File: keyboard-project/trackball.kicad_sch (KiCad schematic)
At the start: 0 parts

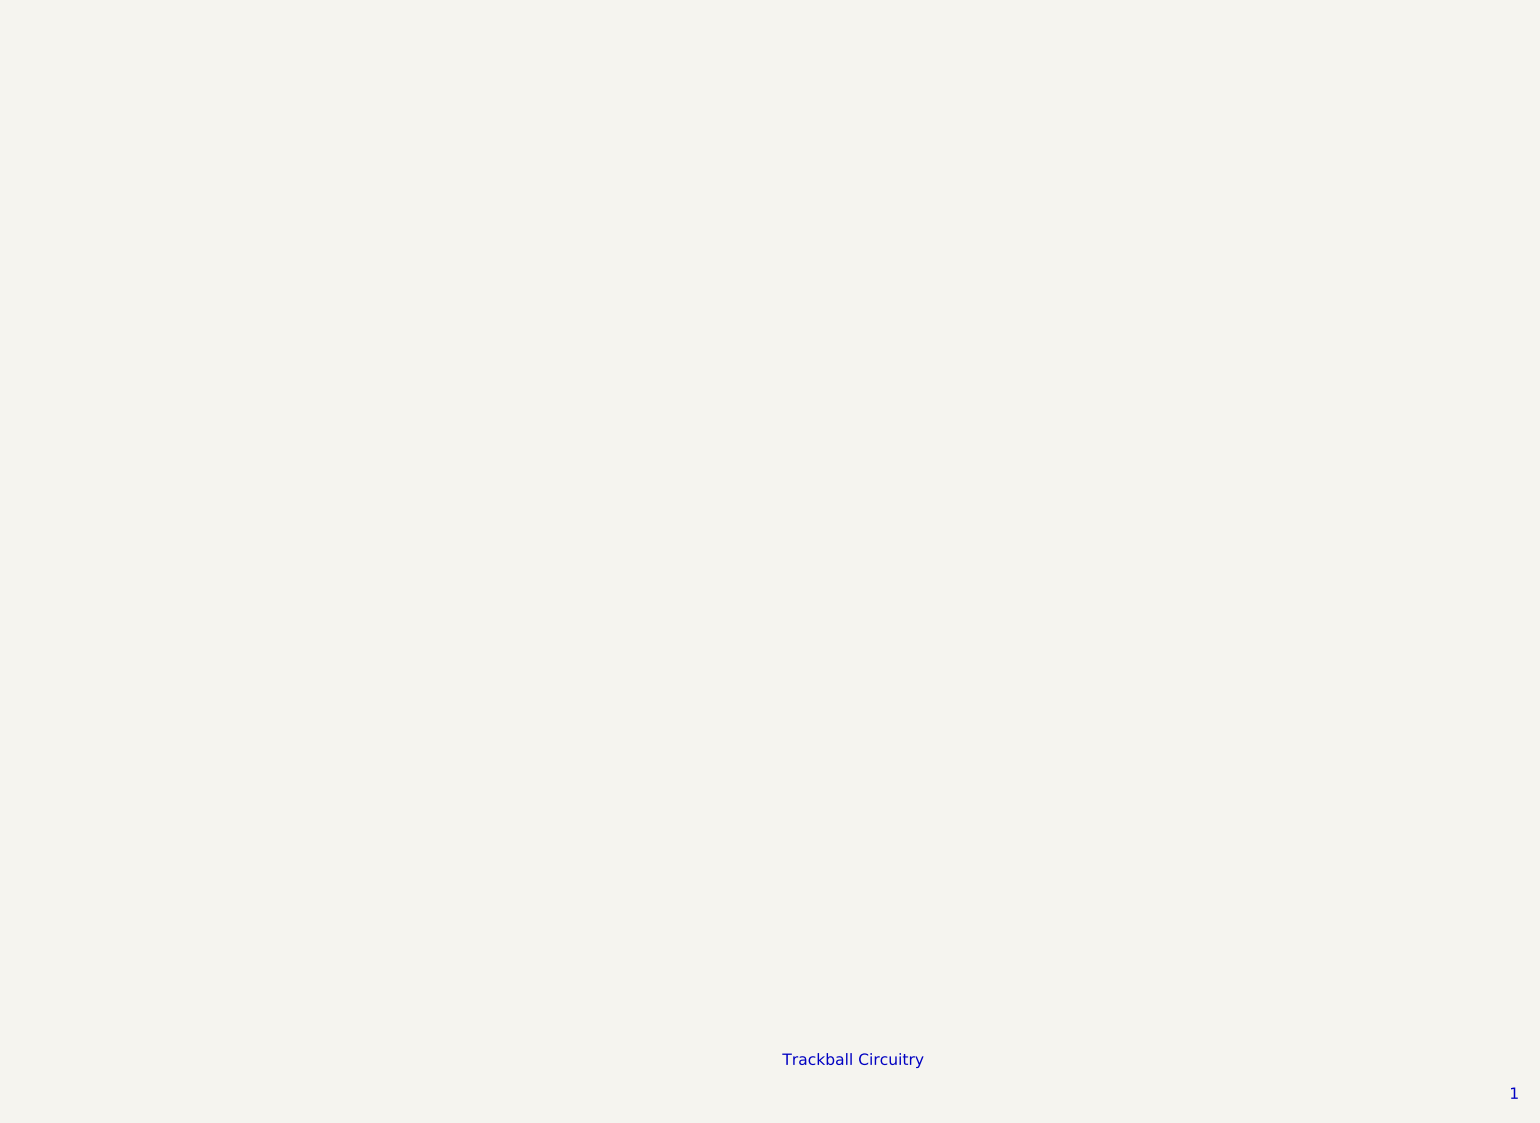
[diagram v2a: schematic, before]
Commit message: encoders, trackball, and display circuits
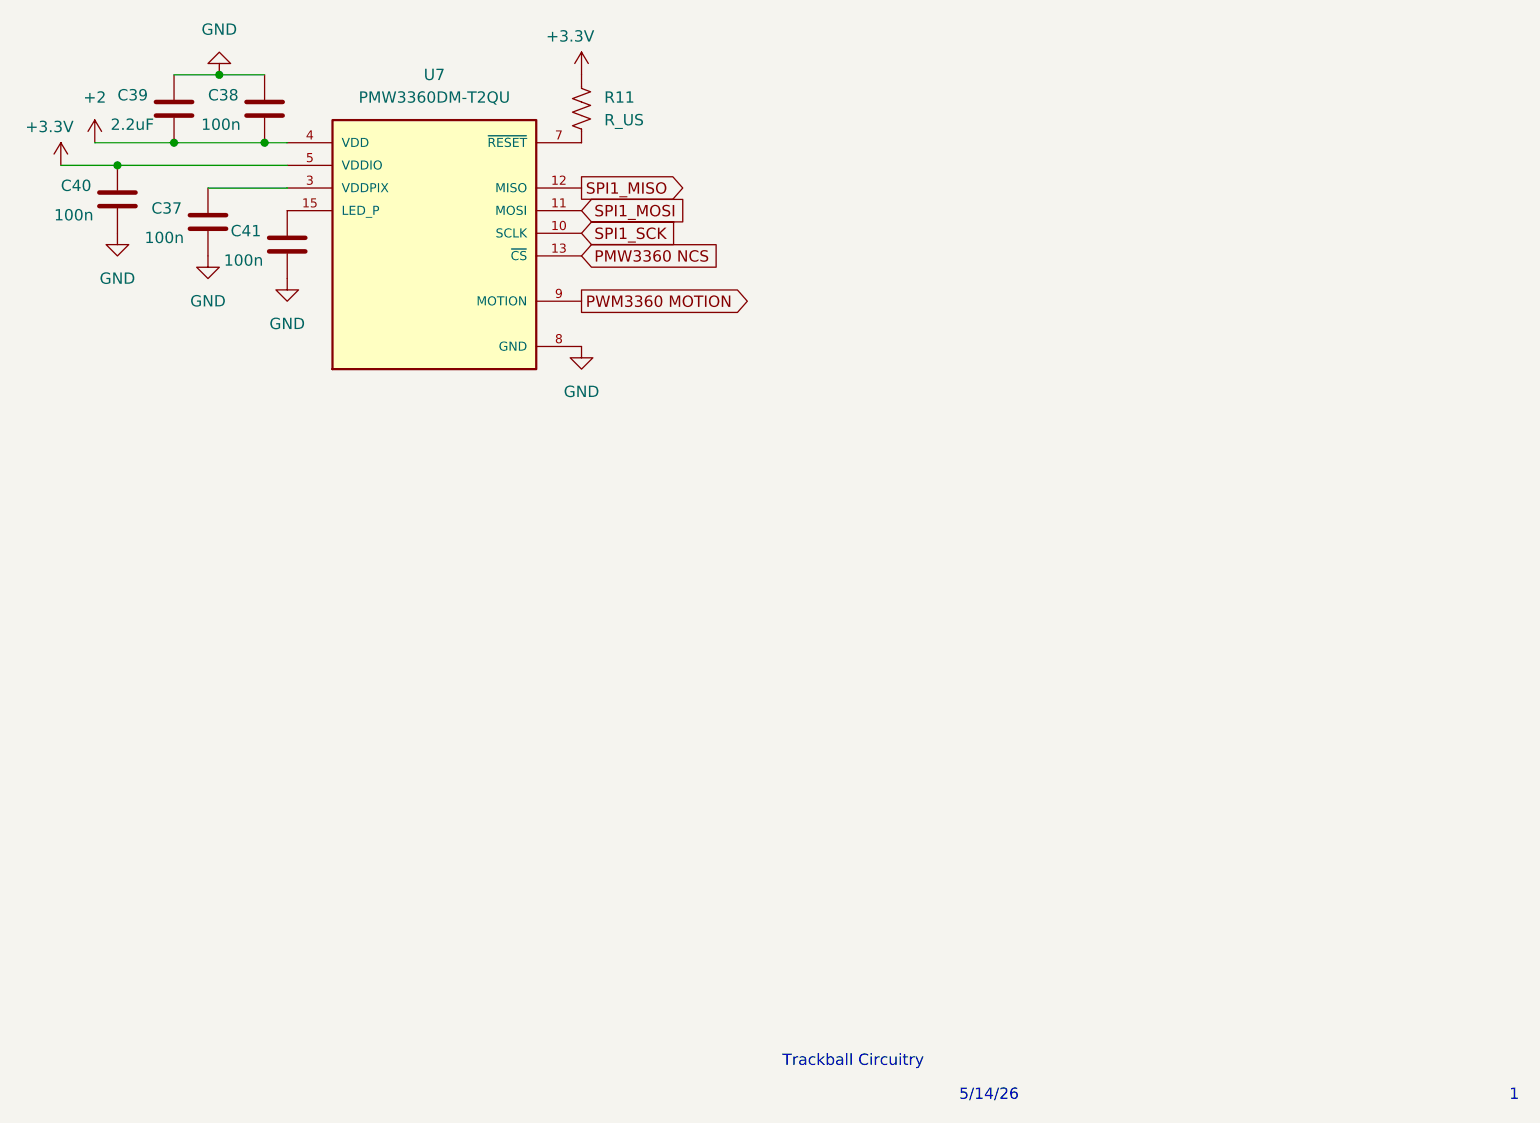
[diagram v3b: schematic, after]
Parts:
- added C37, C38, C40, C41: 100n, symbol Device:C
- added C39: 2.2uF, symbol Device:C
- added R11: R_US, symbol Device:R_US
- added U7: PMW3360DM-T2QU, symbol PMW3360DM-T2QU:PMW3360DM-T2QU
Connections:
- new net: C41.1, U7.15 (LED_P)
- new net: R11.2, U7.7 (~{RESET})
- new net: C37.1, U7.3 (VDDPIX)
- new net +2: C38.2, C39.2, U7.4 (VDD)
- new net +3.3V: C40.1, R11.1, U7.5 (VDDIO)
- new net GND: C37.2, C38.1, C39.1, C40.2, C41.2, U7.8 (GND)
- new net PMW3360 NCS: U7.13 (~{CS})
- new net PWM3360 MOTION: U7.9 (MOTION)
- new net SPI1_MISO: U7.12 (MISO)
- new net SPI1_MOSI: U7.11 (MOSI)
- new net SPI1_SCK: U7.10 (SCLK)
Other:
- note added: "5/14/26"

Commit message: res and cap footprints
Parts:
- C37, C38, C39, C40, C41: footprint (none) -> Capacitor_SMD:C_1206_3216Metric_Pad1.33x1.80mm_HandSolder
- R11: footprint (none) -> Resistor_SMD:R_1206_3216Metric_Pad1.30x1.75mm_HandSolder
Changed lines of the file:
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@@
 			)
 		)
-		(property "Footprint" ""
+		(property "Footprint" "Capacitor_SMD:C_1206_3216Metric_Pad1.33x1.80mm_HandSolder"
 			(at 113.9952 96.52 0)
 			(hide yes)
@@
 			)
 		)
-		(property "Footprint" ""
+		(property "Footprint" "Capacitor_SMD:C_1206_3216Metric_Pad1.33x1.80mm_HandSolder"
 			(at 130.5052 86.36 0)
 			(hide yes)
@@
 			)
 		)
-		(property "Footprint" ""
+		(property "Footprint" "Capacitor_SMD:C_1206_3216Metric_Pad1.33x1.80mm_HandSolder"
 			(at 133.0452 101.6 0)
 			(hide yes)
@@
 			)
 		)
-		(property "Footprint" ""
+		(property "Footprint" "Resistor_SMD:R_1206_3216Metric_Pad1.30x1.75mm_HandSolder"
 			(at 166.116 82.804 90)
 			(hide yes)
@@
 			)
 		)
-		(property "Footprint" ""
+		(property "Footprint" "Capacitor_SMD:C_1206_3216Metric_Pad1.33x1.80mm_HandSolder"
 			(at 120.3452 86.36 0)
 			(hide yes)
@@
 			)
 		)
-		(property "Footprint" ""
+		(property "Footprint" "Capacitor_SMD:C_1206_3216Metric_Pad1.33x1.80mm_HandSolder"
 			(at 124.1552 99.06 0)
 			(hide yes)

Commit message: more footprints
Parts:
- U7: footprint (none) -> PMW3360DM-T2QU:PMW3360
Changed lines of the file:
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@@
 			)
 		)
-		(property "Footprint" ""
+		(property "Footprint" "PMW3360DM-T2QU:PMW3360"
 			(at 149.86 96.52 0)
 			(hide yes)
